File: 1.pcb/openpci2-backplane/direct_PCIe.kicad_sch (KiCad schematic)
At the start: 14 parts, among them J3 BWSMA-KWE-Z001, J5 X3113WVS-64-9TV01, J6 BWSMA-KWE-Z001, J7 AS0BC21-S30BM-7H

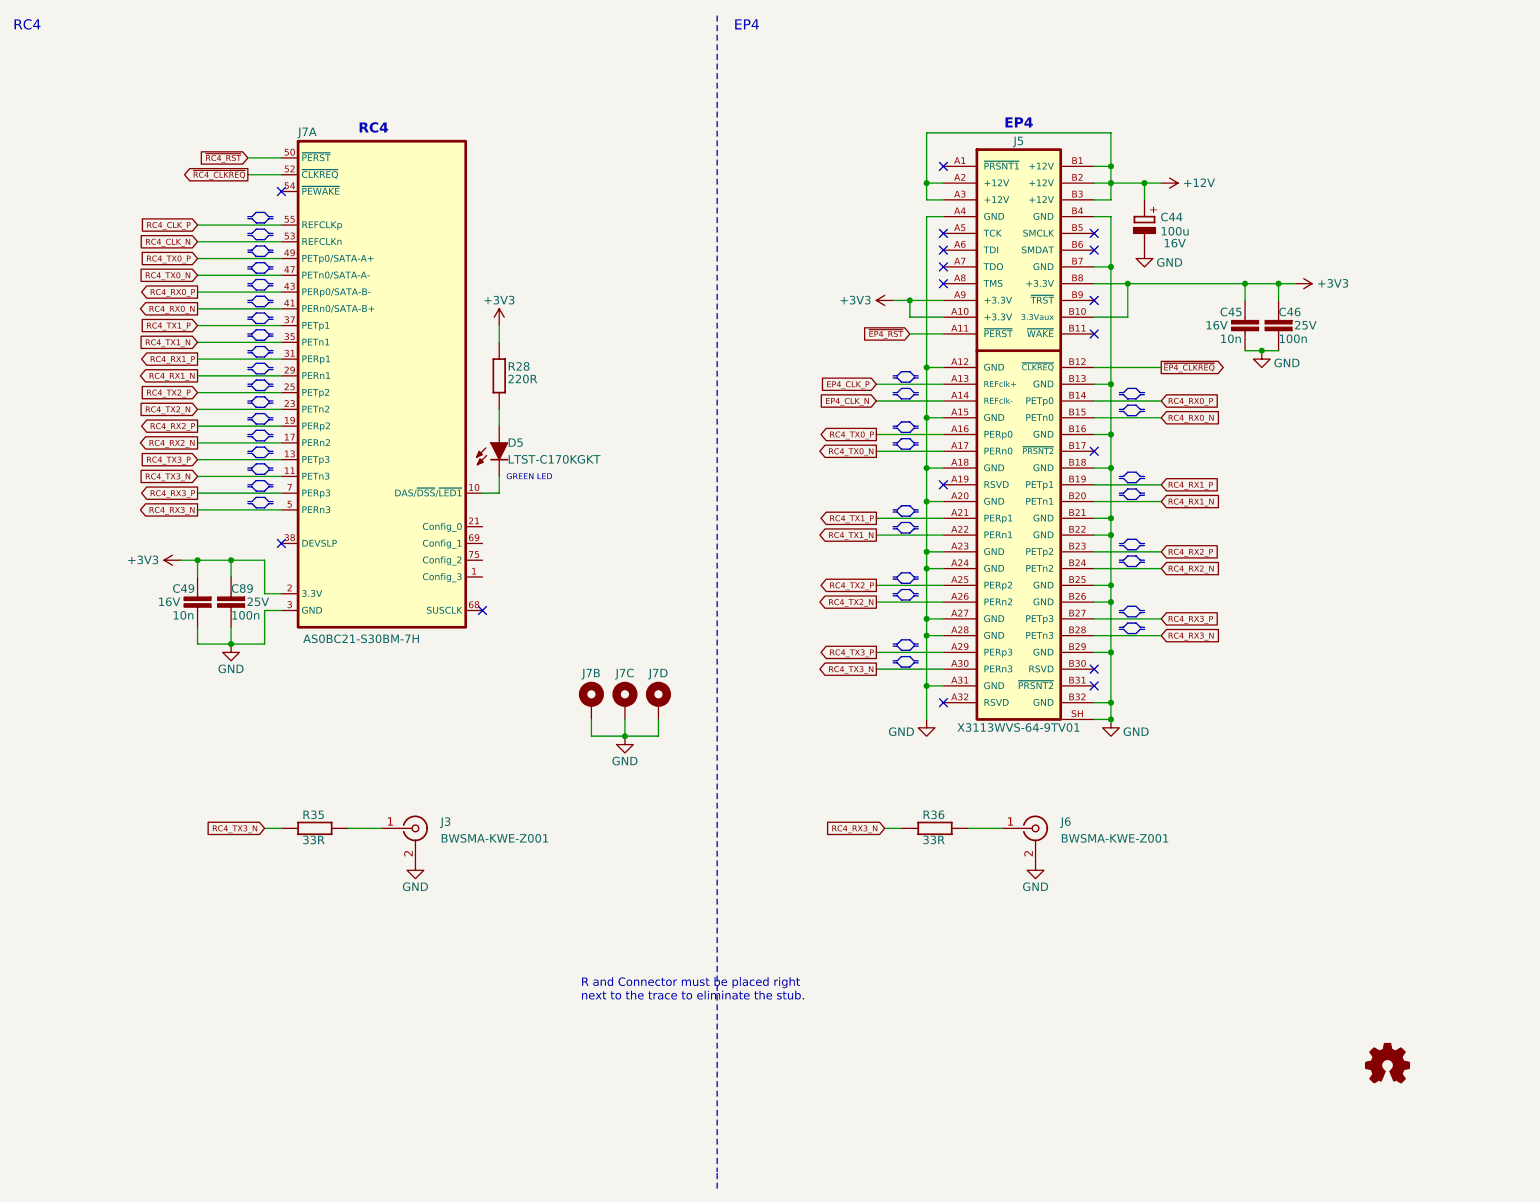
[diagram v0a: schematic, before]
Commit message: SCH and PCB updates in prep for volume production and CrowdSupply campaign
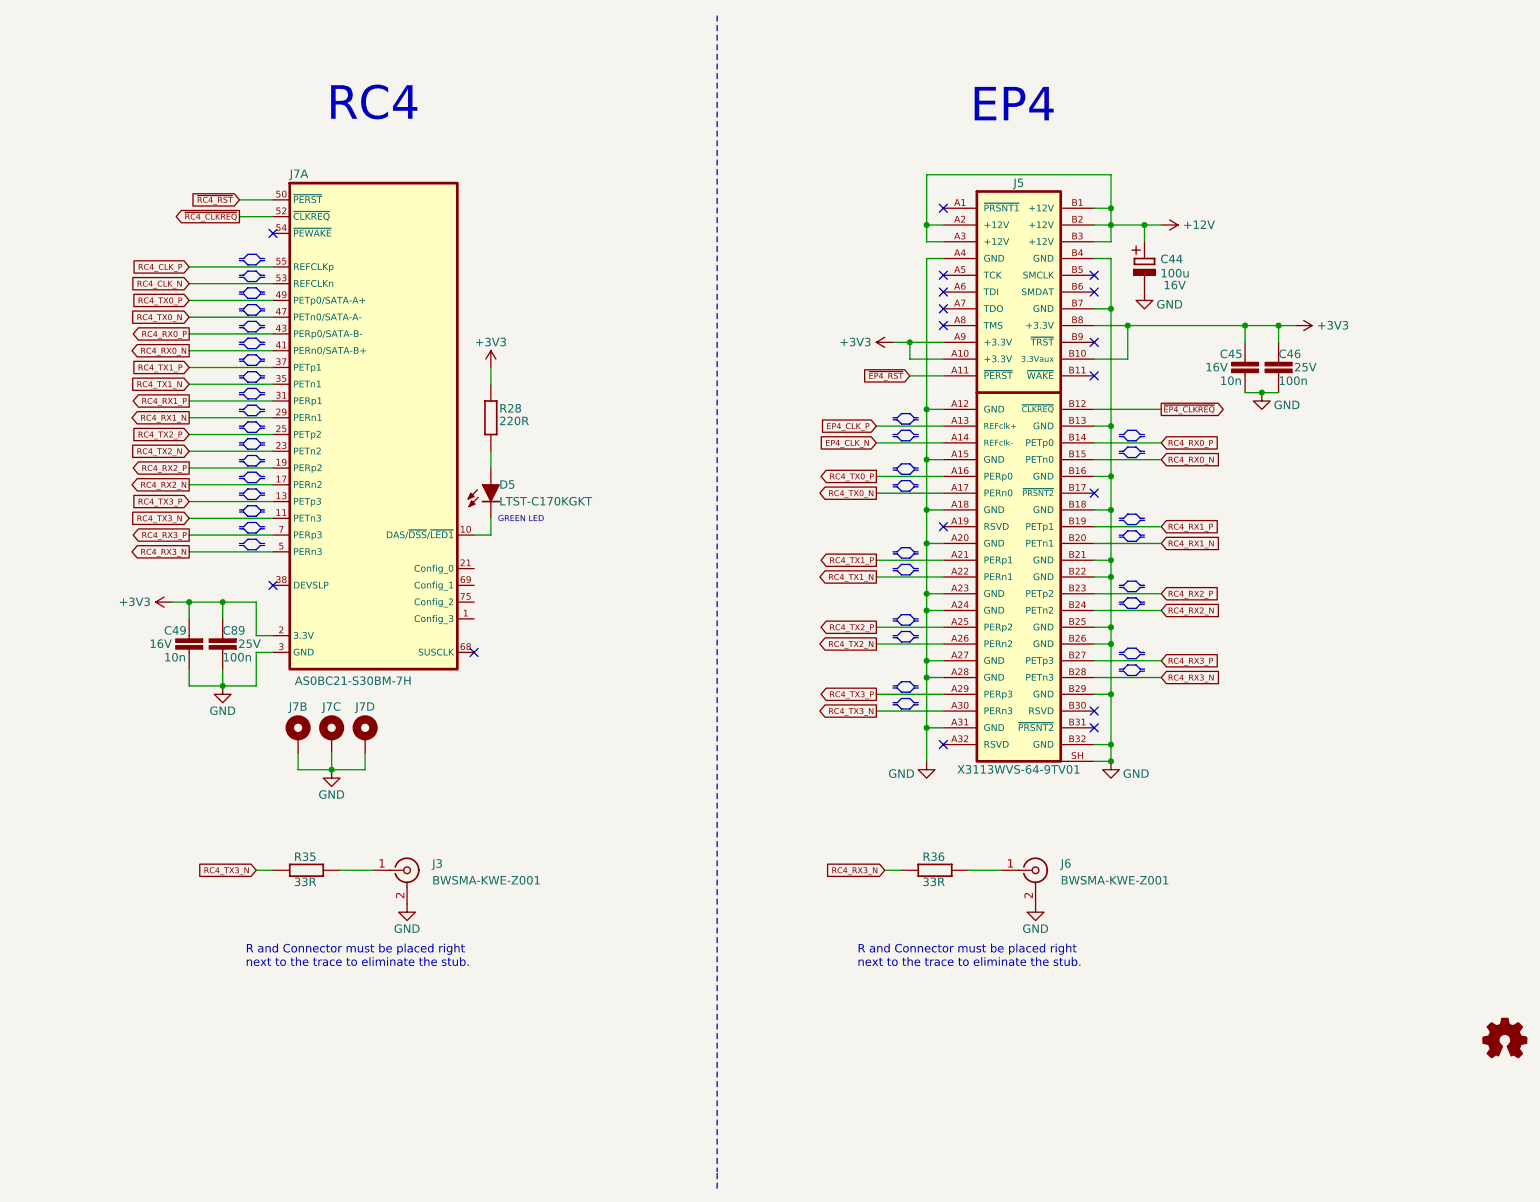
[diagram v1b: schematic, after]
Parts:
- D5: Mouser (none) -> 859-LTST-C170KGKT; TME (none) -> LTST-C170KGKT
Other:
- company: COPYRIGHT (C) Chili.CHIPS.ba doo -> COPYRIGHT (C) CHILI.CHIPS.LLC
- title: (none) -> openPCIE2 Backplane
- moved on the sheet: C45, C46, C49, C89, D5, J3, J5, J6, J7A, J7B, J7C, J7D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

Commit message: Cleanup in prep for the first release
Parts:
- C44: MPN (none) -> EEE-1CA101WAP
- C45, C49: MPN (none) -> GRM155R71C103KA01D
- C46, C89: MPN (none) -> CL05A104KA5NNNC
- D5: MPN (none) -> LTST-C170KGKT
- J3, J6: MPN (none) -> BWSMA-KWE-Z001
- J5: MPN (none) -> X3113WVS-64-9TV01
- J7: MPN (none) -> AS0BC21-S30BM-7H
- R28: MPN (none) -> RC0603JR-07220RL
- R35, R36: MPN (none) -> RMCF0603FT33R0
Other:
- note added: "Direct Connection Island"
- moved on the sheet: D5, R28

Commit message: cleaned up and aligned licensing info with project goal
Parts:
- C44: DigiKey PCE4579CT-ND -> (none)
- C45, C49: DigiKey 490-1313-1-ND -> (none)
- C46, C89: DigiKey 1276-1043-1-ND -> (none)
- D5: DigiKey 160-1414-2-ND -> (none); Mouser 859-LTST-C170KGKT -> (none); TME LTST-C170KGKT -> (none)
- J3, J6: LCSC C496551 -> (none)
- J5: LCSC C5711224 -> (none)
- J7: LCSC C2832351 -> (none)
- R28: DigiKey 311-220GRCT-ND -> (none)
- R35, R36: DigiKey RMCF0603FT33R0CT-ND -> (none)
